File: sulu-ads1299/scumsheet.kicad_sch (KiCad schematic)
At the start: 25 parts, among them J10 through_hole, J11 through_hole, J12 through_hole, J13 through_hole, J14 through_hole, J15 through_hole, J16 through_hole, J17 through_hole, J18 through_hole, J19 through_hole, J20 through_hole, J21 through_hole, J22 through_hole, J6 through_hole, J7 through_hole, J8 through_hole, J9 through_hole, U5 scum3

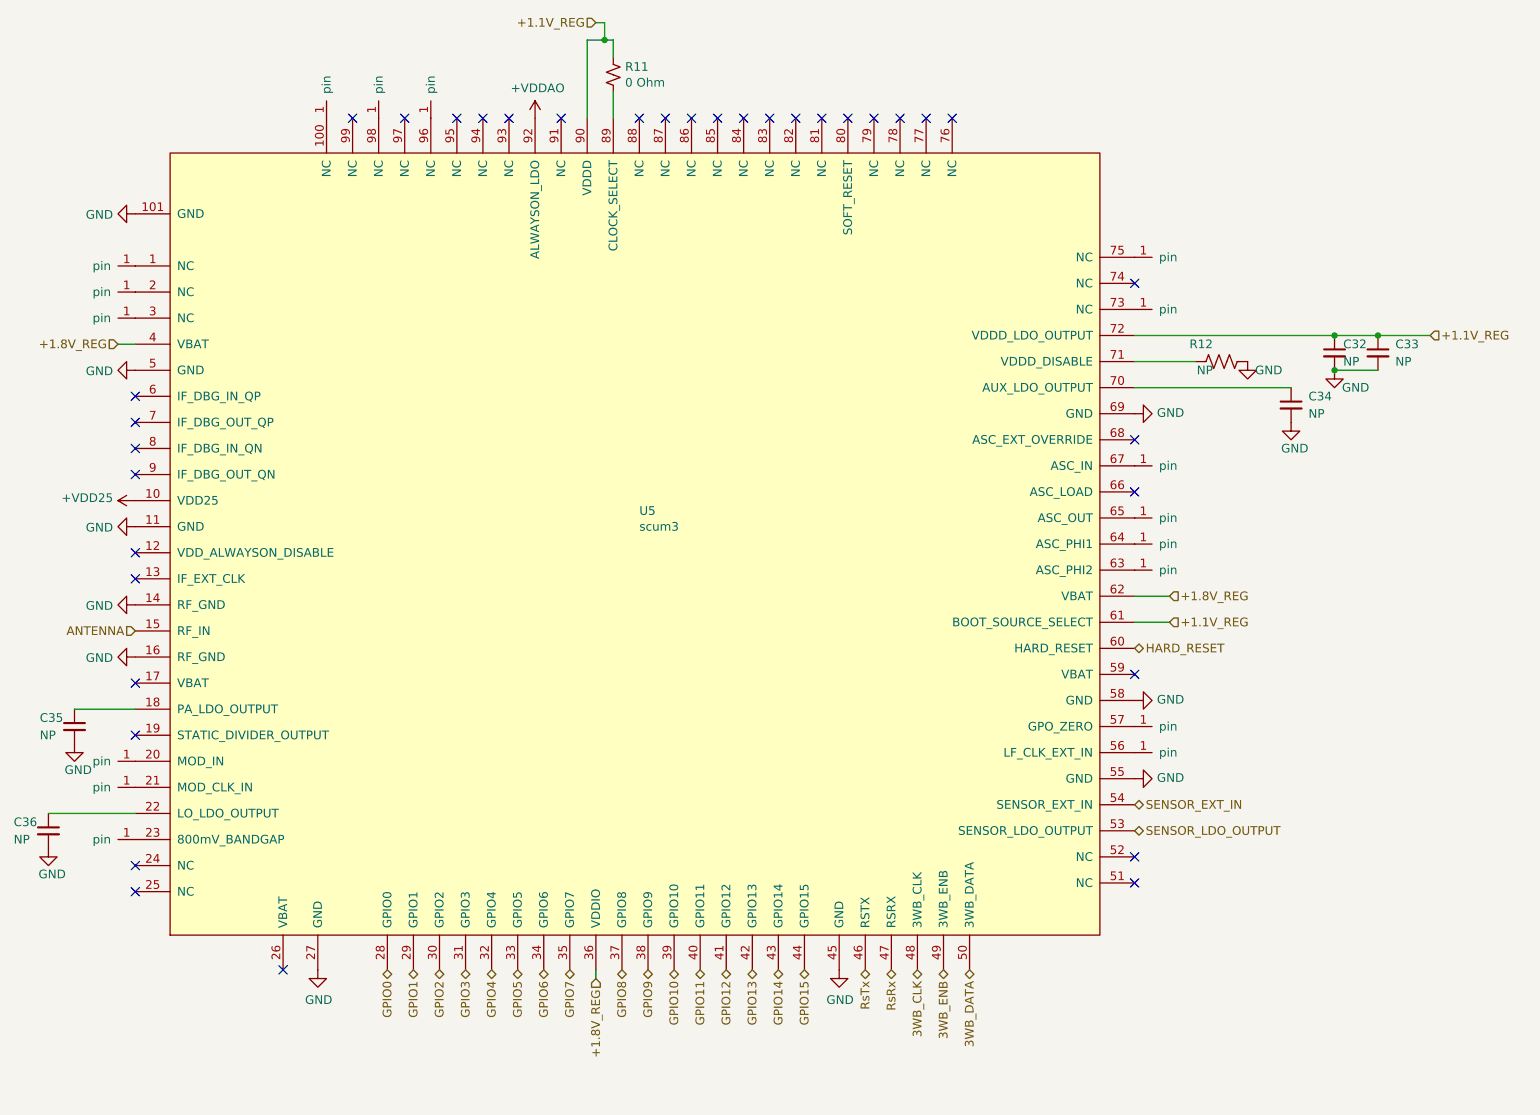
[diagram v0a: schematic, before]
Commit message: Silkscreen cleaned, reduced TP footprint #, post design review
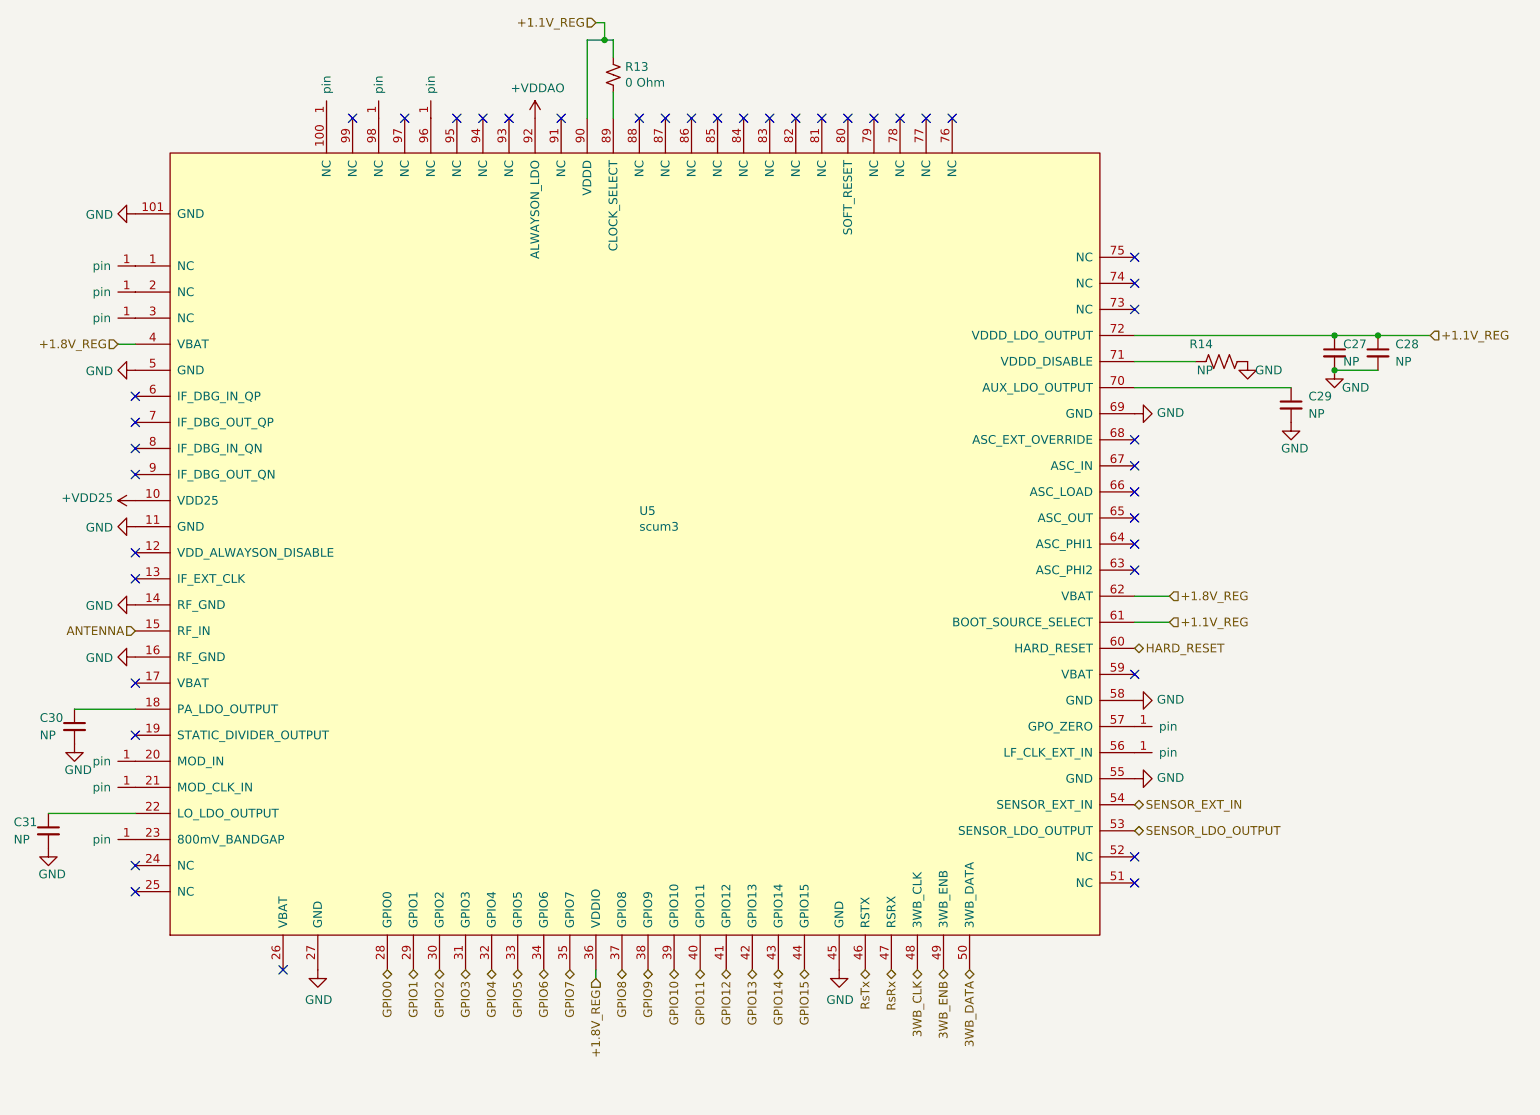
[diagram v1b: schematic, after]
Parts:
- removed J12, J14, J15, J16, J17, J9: through_hole, SCUM:through_hole, symbol draft1library:through_hole
- renumbered C32 to C27, C33 to C28, C34 to C29, C35 to C30, C36 to C31, J13 to J11, J18 to J16, J19 to J17, J20 to J18, J21 to J19, J22 to J20, J6 to J4, J7 to J5, J8 to J6, J10 to J8, J11 to J9, R11 to R13, R12 to R14
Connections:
- no-connect marks 36 -> 42

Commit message: Sulu-ADS1299 rev2 commit before changing 1.1V regulator
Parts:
- removed J18, J19, J9: through_hole, SCUM:through_hole, symbol draft1library:through_hole
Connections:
- no-connect marks 42 -> 45
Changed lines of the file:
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@@
   )
   (no_connect (at 102.87 29.21))
+  (no_connect (at 63.5 54.61))
   (no_connect (at 85.09 153.67))
+  (no_connect (at 63.5 127))
   (no_connect (at 125.73 29.21))
   (no_connect (at 209.55 76.2))
@@
   (no_connect (at 63.5 96.52))
   (no_connect (at 175.26 29.21))
+  (no_connect (at 63.5 123.19))
   (no_connect (at 63.5 73.66))
   (no_connect (at 167.64 29.21))
@@
     (pin "2")
   )
-  (symbol (lib_id "draft1library:through_hole") (at 63.5 127 180) (unit 1)
-    (in_bom yes) (on_board yes)
-    (property "Reference" "J19" (id 0) (at 63.5 132.08 0)
-      (effects (font (size 1.27 1.27)) hide)
-    )
-    (property "Value" "through_hole" (id 1) (at 63.5 129.54 0)
-      (effects (font (size 1.27 1.27)) hide)
-    )
-    (property "Footprint" "SCUM:through_hole" (id 2) (at 63.5 127 0)
-      (effects (font (size 1.27 1.27)) hide)
-    )
-    (property "Datasheet" "" (id 3) (at 63.5 127 0)
-      (effects (font (size 1.27 1.27)) hide)
-    )
-    (pin "1")
-  )
   (symbol (lib_id "power:GND") (at 90.17 153.67 0) (unit 1)
     (in_bom yes) (on_board yes)
@@
     (pin "2")
   )
-  (symbol (lib_id "draft1library:through_hole") (at 63.5 123.19 180) (unit 1)
-    (in_bom yes) (on_board yes)
-    (property "Reference" "J18" (id 0) (at 63.5 128.27 0)
-      (effects (font (size 1.27 1.27)) hide)
-    )
-    (property "Value" "through_hole" (id 1) (at 63.5 125.73 0)
-      (effects (font (size 1.27 1.27)) hide)
-    )
-    (property "Footprint" "SCUM:through_hole" (id 2) (at 63.5 123.19 0)
-      (effects (font (size 1.27 1.27)) hide)
-    )
-    (property "Datasheet" "" (id 3) (at 63.5 123.19 0)
-      (effects (font (size 1.27 1.27)) hide)
-    )
-    (pin "1")
-  )
   (symbol (lib_id "power:GND") (at 63.5 43.18 270) (unit 1)
     (in_bom yes) (on_board yes)
@@
       (effects (font (size 1.27 1.27)) hide)
     )
-    (pin "1")
-  )
-  (symbol (lib_id "draft1library:through_hole") (at 63.5 54.61 180) (unit 1)
-    (in_bom yes) (on_board yes)
-    (property "Reference" "J9" (id 0) (at 63.5 59.69 0)
-      (effects (font (size 1.27 1.27)) hide)
-    )
-    (property "Value" "through_hole" (id 1) (at 63.5 57.15 0)
-      (effects (font (size 1.27 1.27)) hide)
-    )
-    (property "Footprint" "SCUM:through_hole" (id 2) (at 63.5 54.61 0)
-      (effects (font (size 1.27 1.27)) hide)
-    )
-    (property "Datasheet" "" (id 3) (at 63.5 54.61 0)
-      (effects (font (size 1.27 1.27)) hide)
-    )

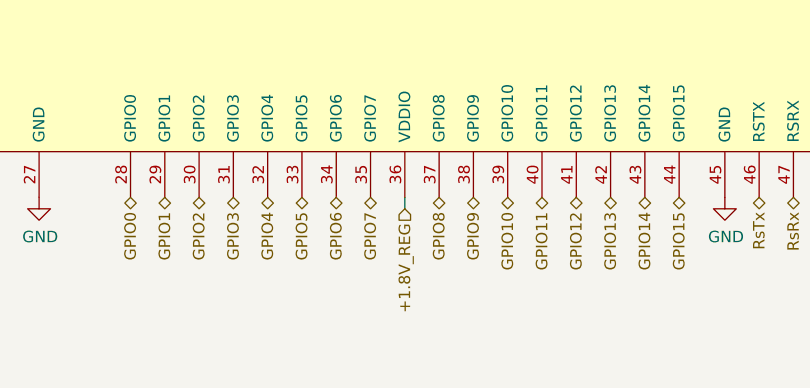
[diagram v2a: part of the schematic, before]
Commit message: BOM adjustments, protection Zener diodes, JLCPCB fab files
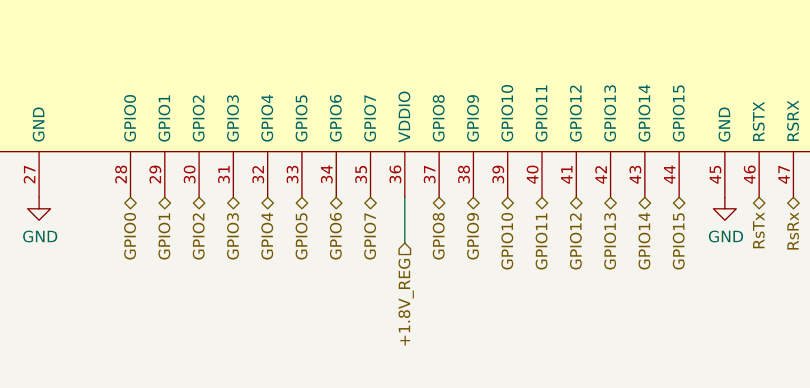
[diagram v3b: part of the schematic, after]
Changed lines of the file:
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@@
     (stroke (width 0) (type default) (color 0 0 0 0))
   )
-  (wire (pts (xy 130.81 153.67) (xy 130.81 154.94))
+  (wire (pts (xy 130.81 153.67) (xy 130.81 158.75))
     (stroke (width 0) (type default) (color 0 0 0 0))
   )
@@
     (effects (font (size 1.27 1.27)) (justify right))
   )
-  (hierarchical_label "+1.8V_REG" (shape input) (at 130.81 154.94 270)
+  (hierarchical_label "+1.8V_REG" (shape input) (at 130.81 158.75 270)
     (effects (font (size 1.27 1.27)) (justify right))
   )

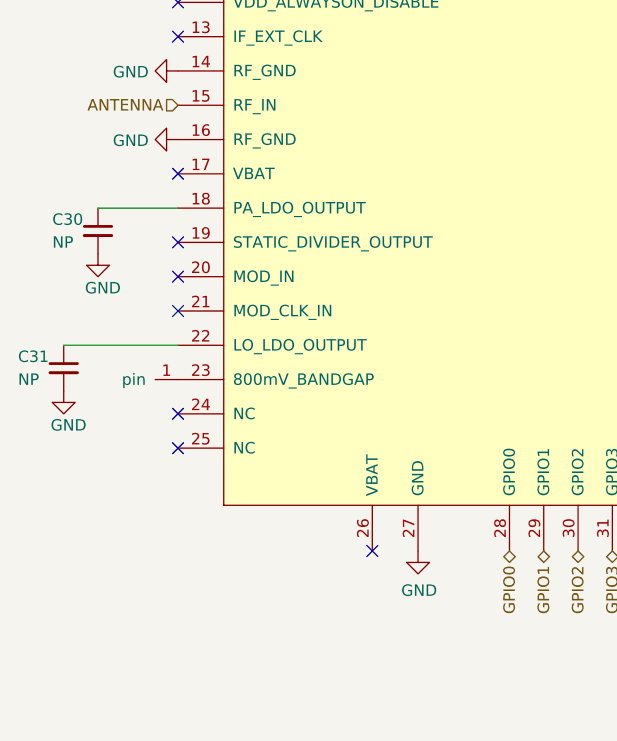
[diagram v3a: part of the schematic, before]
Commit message: Sulu-ADS1299 Rev 3 improved routing surrounding QFN
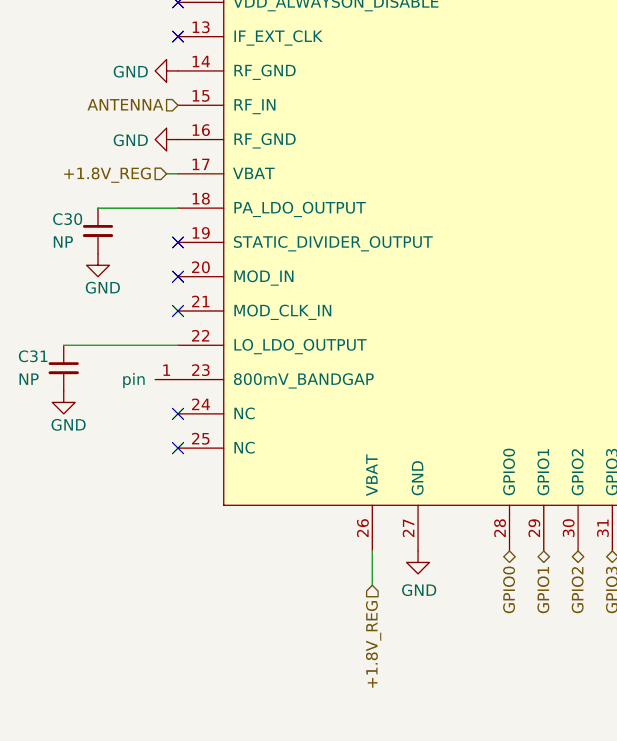
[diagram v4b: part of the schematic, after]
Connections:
- net +1.8V_REG: now also U5.17 (VBAT), U5.26 (VBAT)
- no-connect marks 45 -> 43
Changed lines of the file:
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@@
   (no_connect (at 102.87 29.21))
   (no_connect (at 63.5 54.61))
-  (no_connect (at 85.09 153.67))
   (no_connect (at 63.5 127))
   (no_connect (at 125.73 29.21))
@@
   (no_connect (at 63.5 77.47))
   (no_connect (at 160.02 29.21))
-  (no_connect (at 63.5 111.76))
   (no_connect (at 163.83 29.21))
   (no_connect (at 63.5 92.71))
@@
     (stroke (width 0) (type default) (color 0 0 0 0))
   )
+  (wire (pts (xy 85.09 153.67) (xy 85.09 157.48))
+    (stroke (width 0) (type default) (color 0 0 0 0))
+  )
   (wire (pts (xy 130.81 15.24) (xy 132.08 15.24))
+    (stroke (width 0) (type default) (color 0 0 0 0))
+  )
+  (wire (pts (xy 62.23 111.76) (xy 63.5 111.76))
     (stroke (width 0) (type default) (color 0 0 0 0))
   )
@@
     (effects (font (size 1.27 1.27)) (justify right))
   )
+  (hierarchical_label "+1.8V_REG" (shape input) (at 85.09 157.48 270)
+    (effects (font (size 1.27 1.27)) (justify right))
+  )
   (hierarchical_label "ANTENNA" (shape input) (at 63.5 104.14 180)
     (effects (font (size 1.27 1.27)) (justify right))
@@
     (effects (font (size 1.27 1.27)) (justify right))
   )
+  (hierarchical_label "+1.8V_REG" (shape input) (at 62.23 111.76 180)
+    (effects (font (size 1.27 1.27)) (justify right))
+  )
